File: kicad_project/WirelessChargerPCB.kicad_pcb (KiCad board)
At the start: 4 copper layers, 27 parts, among them J1 Screw_Terminal_01x02, J2 Screw_Terminal_01x02, J3 Conn_01x02_Socket, J5 Conn_01x02_Socket, Q1 BD139, Q2 IRFZ44N, U1 NE555D

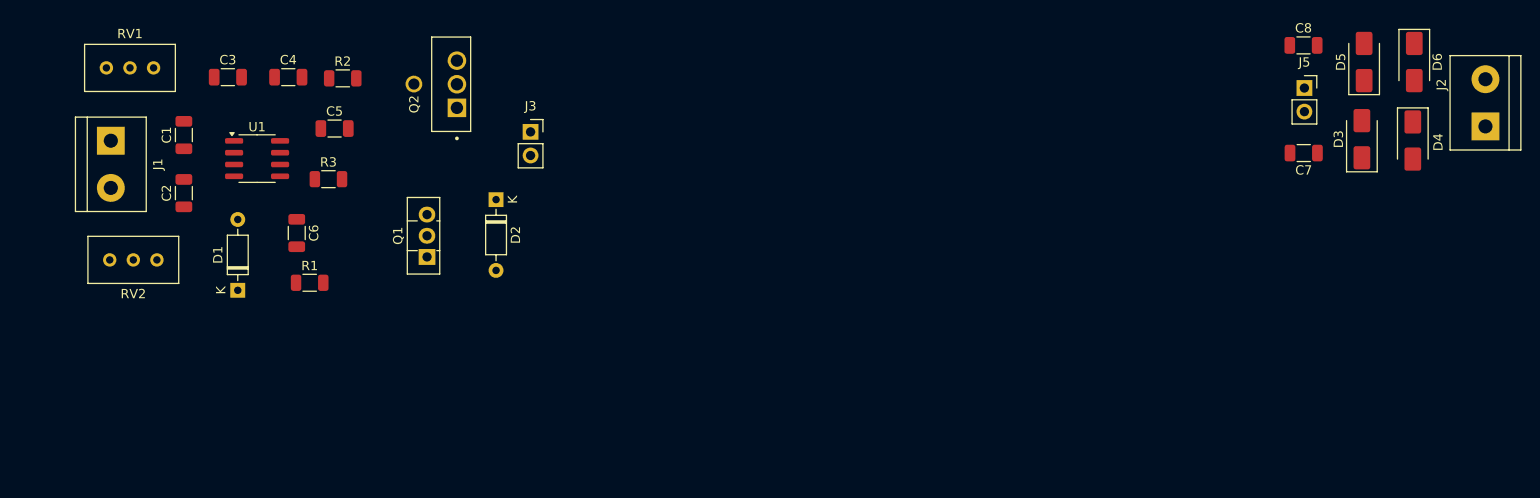
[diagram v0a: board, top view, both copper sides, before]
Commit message: Agregando huellas de Heatsinks y relizando acomodo de ambas PCBs
Signed-off-by: RoMadrigal <rmadrigalmontes@gmail.com>
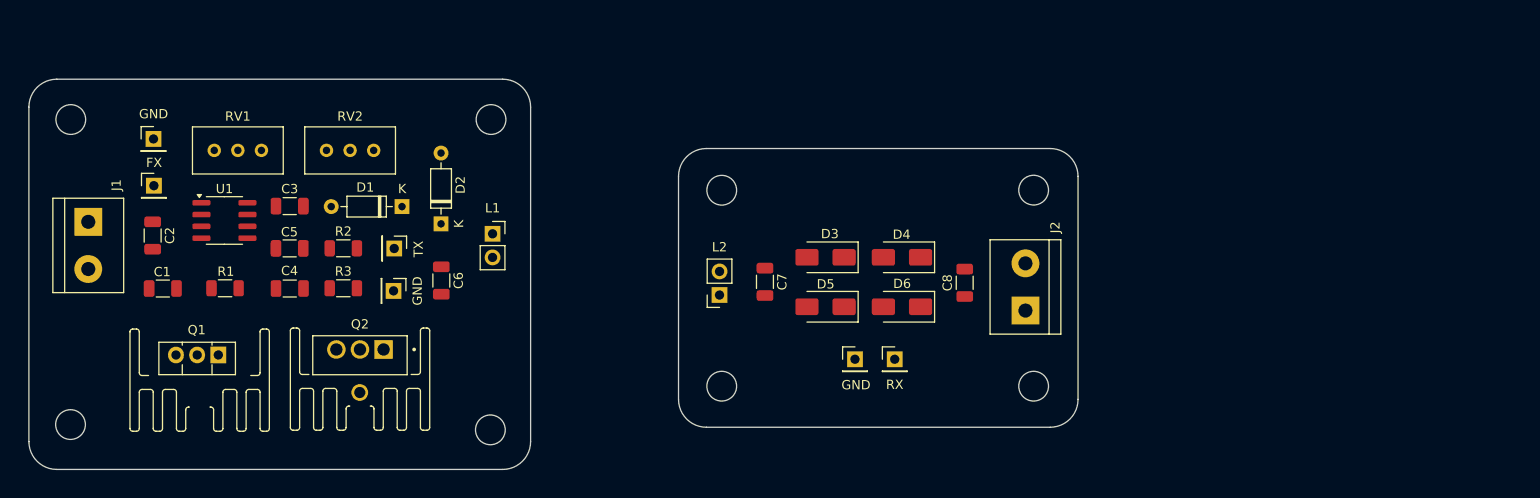
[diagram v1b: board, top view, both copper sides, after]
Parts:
- added REF**: MountingHole_3.2mm_M3, MountingHole:MountingHole_3.2mm_M3, F.Cu at (139.8, 82.7)
- added REF**: MountingHole_3.2mm_M3, MountingHole:MountingHole_3.2mm_M3, F.Cu at (164.6, 111.4)
- added REF**: MountingHole_3.2mm_M3, MountingHole:MountingHole_3.2mm_M3, F.Cu at (198.2, 90.3)
- added REF**: MountingHole_3.2mm_M3, MountingHole:MountingHole_3.2mm_M3, F.Cu at (139.7, 116.1)
- added REF**: MountingHole_3.2mm_M3, MountingHole:MountingHole_3.2mm_M3, F.Cu at (198.2, 111.4)
- added REF**: MountingHole_3.2mm_M3, MountingHole:MountingHole_3.2mm_M3, F.Cu at (94.5, 115.6)
- added REF**: MountingHole_3.2mm_M3, MountingHole:MountingHole_3.2mm_M3, F.Cu at (94.5, 82.7)
- added REF**: MountingHole_3.2mm_M3, MountingHole:MountingHole_3.2mm_M3, F.Cu at (164.6, 90.3)
- added REF**: Heatsink_TO220_Vert_20x15x11_Pin1, Huellas:Heatsink_TO220_Vert_20x15x11_Pin1, F.Cu at (108.4, 110.8)
- added REF**: Heatsink_TO220_Vert_20x15x11_Pin1, Huellas:Heatsink_TO220_Vert_20x15x11_Pin1, F.Cu at (125.7, 110.7)
- added TP1: GND, Connector_PinHeader_2.54mm:PinHeader_1x01_P2.54mm_Vertical, F.Cu at (103.4, 84.8)
- added TP2: OutTim, Connector_PinHeader_2.54mm:PinHeader_1x01_P2.54mm_Vertical, F.Cu at (103.5, 89.9)
- added TP3: TX, Connector_PinHeader_2.54mm:PinHeader_1x01_P2.54mm_Vertical, F.Cu at (129.3, 96.6)
- added TP4: RX, Connector_PinHeader_2.54mm:PinHeader_1x01_P2.54mm_Vertical, F.Cu at (183.2, 108.5)
- added TP5: GND, Connector_PinHeader_2.54mm:PinHeader_1x01_P2.54mm_Vertical, F.Cu at (129.3, 101.2)
- added TP6: GND, Connector_PinHeader_2.54mm:PinHeader_1x01_P2.54mm_Vertical, F.Cu at (178.9, 108.5)
- moved L2 66.8 mm to (164.4, 101.6), turned to 180 degrees
- moved D5 63.7 mm to (175.8, 102.9), turned to 180 degrees
- moved D6 61.1 mm to (184.0, 102.9), turned to 180 degrees
- moved C7 59.6 mm to (169.2, 100.2), turned to -90 degrees
- moved D3 59.1 mm to (175.8, 97.6), turned to 180 degrees
- moved D4 56.4 mm to (184.0, 97.6), turned to 180 degrees
- moved J2 53.3 mm to (197.3, 103.3)
- moved C8 44.5 mm to (190.7, 100.3), turned to 90 degrees
- moved REF** 33.7 mm to (125.7, 112.1), turned to 180 degrees
- moved RV2 30.8 mm to (127.1, 86.1), turned to 0 degrees
- moved Q2 30.4 mm to (125.7, 107.5), turned to 180 degrees
- moved Q1 24.8 mm to (110.4, 108.1), turned to 180 degrees
- moved C4 22.8 mm to (118.1, 100.9), turned to 180 degrees
- moved D1 19.8 mm to (130.2, 92.1), turned to 180 degrees
- moved R2 18.3 mm to (123.9, 96.6)
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- renumbered J3 to L1, J5 to L2
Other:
- board outline added: 112.9 x 42 mm
- board text added: "FX"
- board text added: "GND"
- board text added: "RX"
- board text added: "TX"

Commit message: Ruteando y agregando detalles en Silkscreen en ambas PCBs
Signed-off-by: RoMadrigal <rmadrigalmontes@gmail.com>
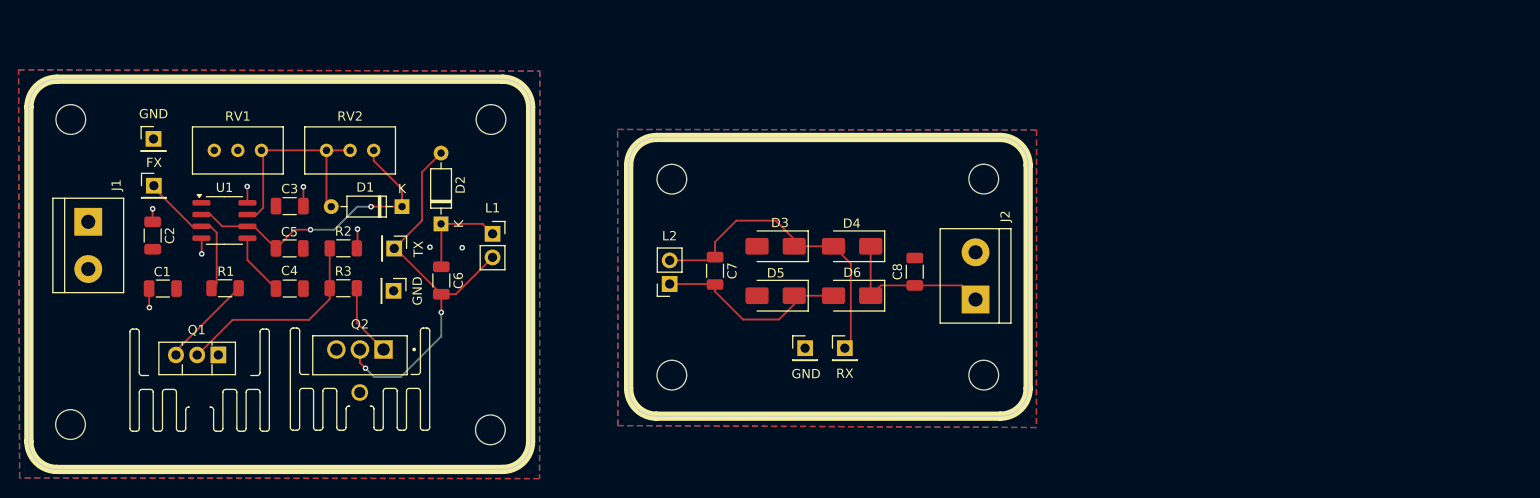
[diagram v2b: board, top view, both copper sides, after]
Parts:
- added kibuzzard-69159BA1: G***, kibuzzard-69159BA1, B.Cu at (101.7, 98.8)
- added kibuzzard-69159BFD: G***, kibuzzard-69159BFD, B.Cu at (101.7, 94.6)
- added kibuzzard-69159C7D: G***, kibuzzard-69159C7D, B.Cu at (186.8, 102.2)
- added kibuzzard-69159C9A: G***, kibuzzard-69159C9A, B.Cu at (186.6, 97.2)
- moved TP4 5.50 mm to (177.8, 107.3)
- moved TP6 5.50 mm to (173.6, 107.3)
- moved C7 5.50 mm to (163.9, 99.0)
- moved C8 5.50 mm to (185.4, 99.1)
- moved D4 5.50 mm to (178.6, 96.4)
- moved D6 5.50 mm to (178.6, 101.7)
- moved J2 5.50 mm to (191.9, 102.1)
- moved REF** 5.50 mm to (159.2, 110.2)
- moved REF** 5.50 mm to (192.8, 89.2)
- moved REF** 5.50 mm to (192.8, 110.2)
- moved REF** 5.50 mm to (159.2, 89.2)
- moved D3 5.50 mm to (170.4, 96.4)
- moved D5 5.50 mm to (170.4, 101.7)
- moved L2 5.50 mm to (159.0, 100.4)
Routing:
- net Net-(D2-A): track 0.00 -> 43.8 mm, vias 0 -> 2
- net Net-(D3-K): track 0.00 -> 34.0 mm
- net Net-(D1-K): track 0.00 -> 32.3 mm, vias 0 -> 2
- net Net-(D1-A): track 0.00 -> 24.4 mm
- net Net-(Q1-C): track 0.00 -> 22.2 mm
- net Net-(D5-K): track 0.00 -> 21.3 mm
- net Net-(D4-K): track 0.00 -> 17.7 mm
- net Out_Timer: track 0.00 -> 15.2 mm
- net +9V: track 0.00 -> 11.1 mm, vias 0 -> 6
- net Net-(D2-K): track 0.00 -> 10.6 mm
- net Net-(Q1-B): track 0.00 -> 9.97 mm
- net Net-(Q2-Pad1): track 0.00 -> 7.78 mm
- net Net-(U1-CV): track 0.00 -> 6.70 mm
- net GND: vias 0 -> 2
- added copper zone on In1.Cu, net +9V
- added copper zone on B.Cu, net GND
- added copper zone on F.Cu, net GND
- added copper zone on In1.Cu, net GND
- added copper zone on In2.Cu, net GND
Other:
- board size 112.9 x 42 mm -> 107.5 x 42 mm

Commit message: Agregando informacion importante al silkcreem ademas del agujero de montaje para el disipador asi como una reconfiguracion a la placa del circuito transmisor
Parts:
- added G***: LOGO, Huellas:QR_project, B.Cu at (175.0, 96.7)
- added G***: LOGO, Huellas:capibara4, B.Cu at (115.7, 101.1)
- added REF**: MountingHole_D1.2, Huellas:MountingHole_D1.2, F.Cu at (108.3, 112.5)
- moved REF** 0.18 mm to (125.6, 112.3), turned to 0 degrees
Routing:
- net GND: vias 2 -> 3
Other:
- board size 107.5 x 42 mm -> 107.6 x 42 mm
- board text added: "anthonycalvo50@gmail.com"
- board text added: "rmadrigalmontes@gmail.com"

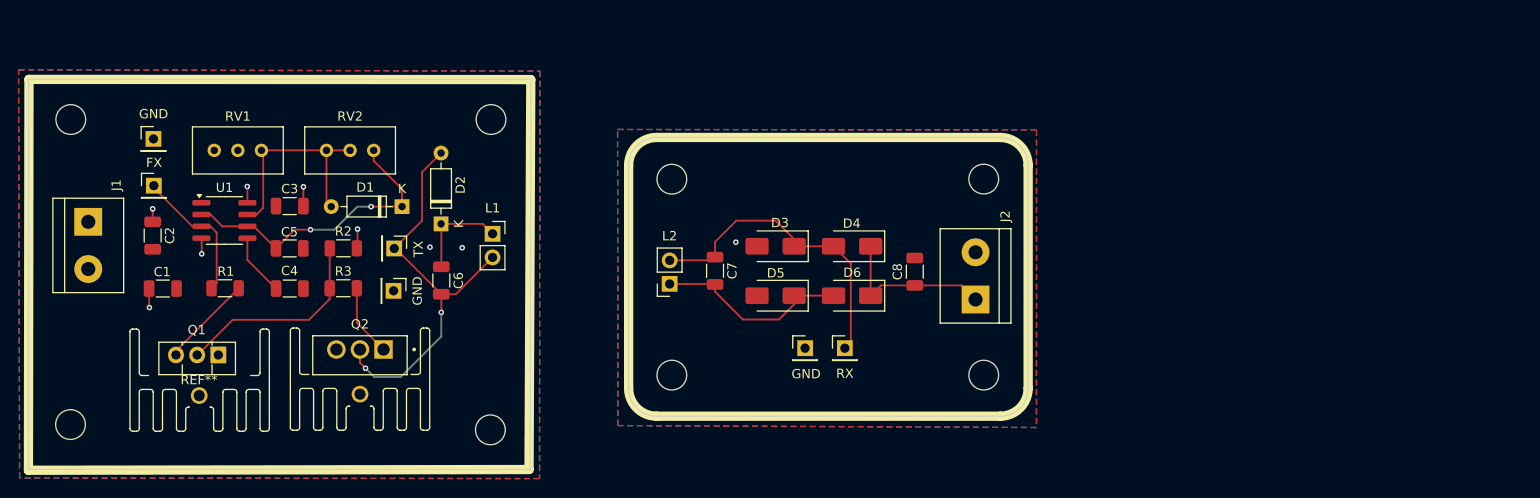
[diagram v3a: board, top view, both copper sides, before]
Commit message: Agregando mouse-bites y logos en ambas PCBs
Signed-off-by: RoMadrigal <rmadrigalmontes@gmail.com>
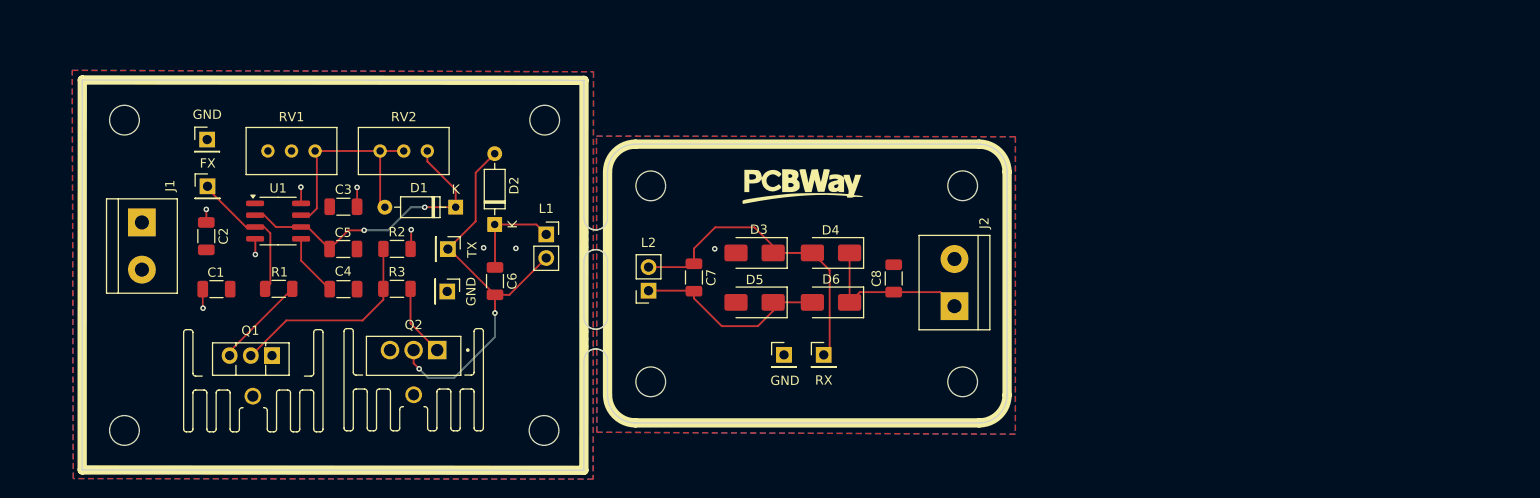
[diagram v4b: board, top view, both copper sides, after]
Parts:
- added G***: LOGO, Huellas:pcbway, F.Cu at (173.3, 90.0)
- added G***: LOGO, Huellas:fish1, B.Cu at (122.2, 98.7)
- added mouse-bite-2.54mm-slot: VAL**, MouseBites:mouse-bite-2.54mm-slot, F.Cu at (151.0, 106.4)
- added mouse-bite-2.54mm-slot: VAL**, MouseBites:mouse-bite-2.54mm-slot, F.Cu at (151.0, 95.7)
- moved G*** 9.54 mm to (122.2, 108.1)
- moved REF** 5.84 mm to (100.3, 116.2)
- moved C4 5.78 mm to (123.9, 101.0)
- moved C5 5.78 mm to (123.9, 96.7)
- moved C6 5.78 mm to (140.2, 100.1)
- moved D1 5.78 mm to (136.0, 92.2)
- moved D2 5.78 mm to (140.2, 94.0)
- moved J1 5.78 mm to (102.2, 93.8)
- moved Q1 5.78 mm to (116.2, 108.1)
- moved Q2 5.78 mm to (131.4, 107.6)
- moved REF** 5.78 mm to (145.5, 82.8)
- moved REF** 5.78 mm to (131.4, 110.7)
- moved REF** 5.78 mm to (145.5, 116.2)
- moved REF** 5.78 mm to (114.1, 112.5)
- moved REF** 5.78 mm to (100.3, 82.8)
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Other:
- board size 107.6 x 42 mm -> 99.5 x 42 mm

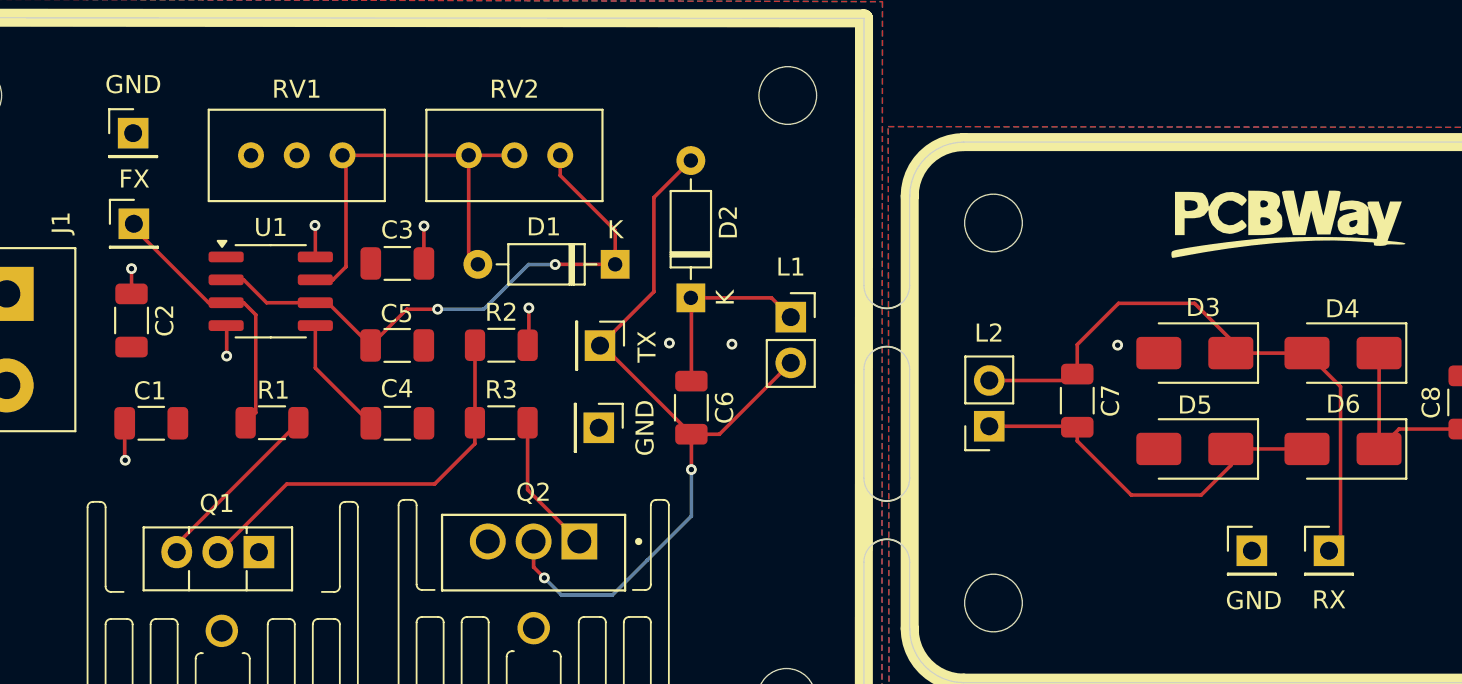
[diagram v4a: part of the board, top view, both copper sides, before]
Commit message: Agregando nuevos puntos de prueba y corrigiendo +9V faltante
Signed-off-by: RoMadrigal <rmadrigalmontes@gmail.com>
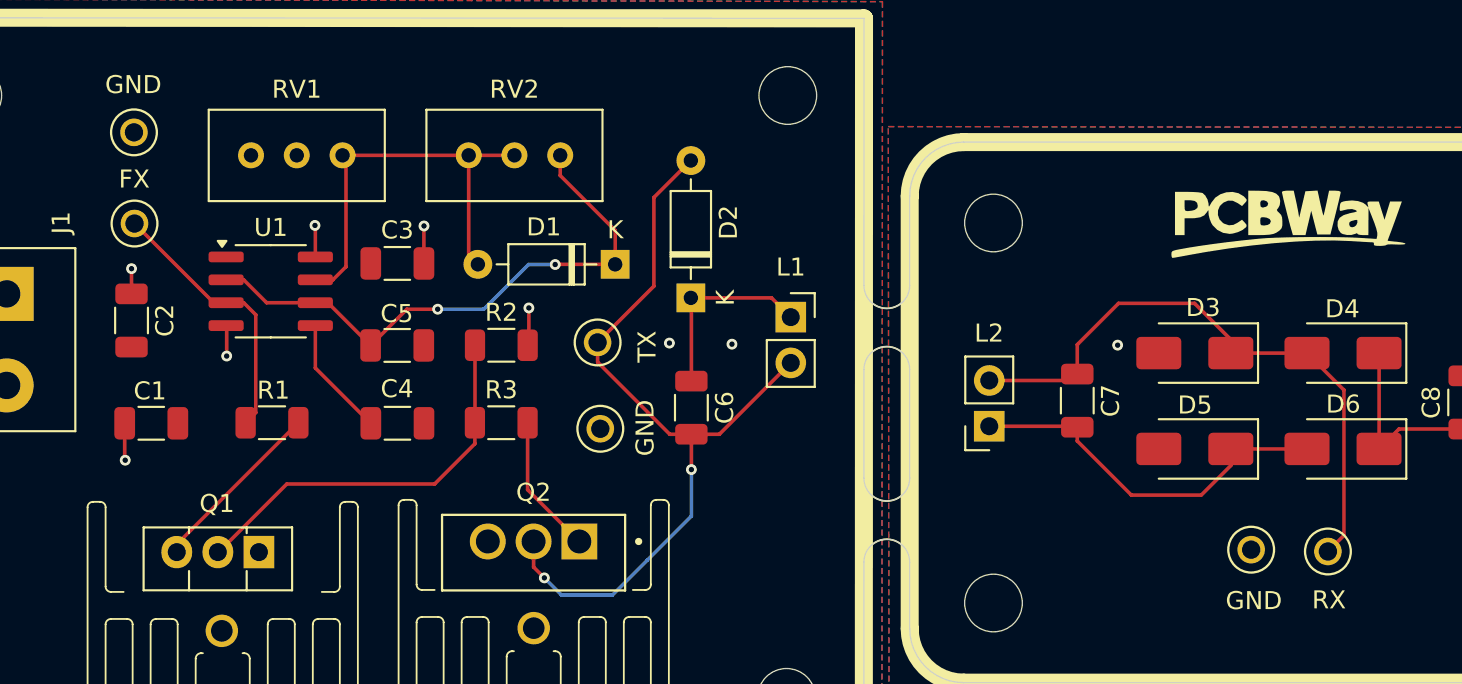
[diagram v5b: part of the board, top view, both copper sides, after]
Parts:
- TP1, TP2, TP4, TP6: footprint Connector_PinHeader_2.54mm:PinHeader_1x01_P2.54mm_Vertical -> TestPoint:KEYSTONE_5263
- TP3: value TX -> GND; footprint Connector_PinHeader_2.54mm:PinHeader_1x01_P2.54mm_Vertical -> TestPoint:KEYSTONE_5263
- TP5: value GND -> TX; footprint Connector_PinHeader_2.54mm:PinHeader_1x01_P2.54mm_Vertical -> TestPoint:KEYSTONE_5263
- moved TP5 4.74 mm to (135.0, 96.5), turned to 0 degrees
- moved TP3 4.62 mm to (135.1, 101.3), turned to 0 degrees
- moved TP4 0.07 mm to (175.5, 108.1)
- moved TP6 0.07 mm to (171.2, 108.0)
- moved TP1 0.06 mm to (109.2, 84.8)
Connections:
- C6 pad 1: Net-(D2-K) -> +9V
- D2 pad 1: Net-(D2-K) -> +9V
- L1 pad 1: Net-(D2-K) -> +9V
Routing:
- net Net-(D2-K): track 10.6 -> 0.00 mm
- net +9V: track 11.1 -> 21.7 mm
- net Net-(D2-A): track 43.8 -> 44.5 mm
